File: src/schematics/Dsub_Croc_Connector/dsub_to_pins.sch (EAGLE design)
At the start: 39 parts

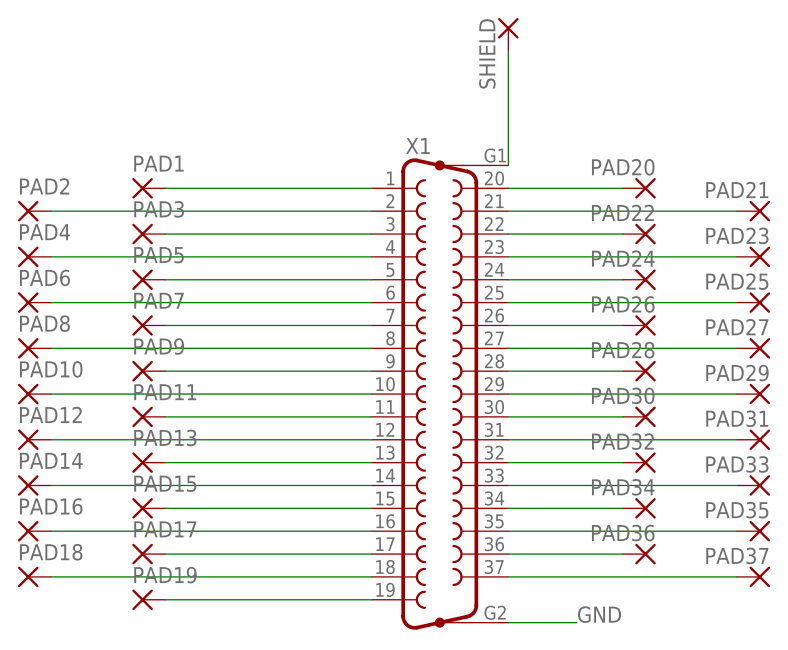
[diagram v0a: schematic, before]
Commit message: New Debug phantom, and new Dsub adaptors. With Gerbers sent to PCBWay
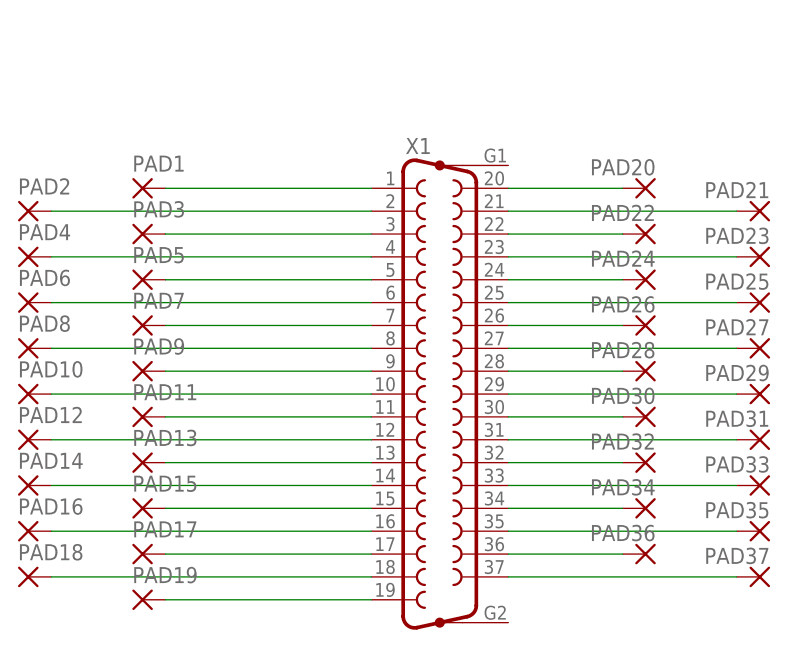
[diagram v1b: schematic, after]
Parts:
- removed SHIELD: WIREPAD3,81/1,3, wirepad:WIREPAD3,81/1,3
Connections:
- removed net GND: SHIELD.P, X1.G1, X1.G2
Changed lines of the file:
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@@
 <part name="PAD36" library="wirepad" deviceset="WIREPAD" device="3,81/1,3" value="WIREPAD3,81/1,3"/>
 <part name="PAD37" library="wirepad" deviceset="WIREPAD" device="3,81/1,3" value="WIREPAD3,81/1,3"/>
-<part name="SHIELD" library="wirepad" deviceset="WIREPAD" device="3,81/1,3" value="WIREPAD3,81/1,3"/>
 </parts>
 <sheets>
@@
 <attribute name="NAME" x="148.463" y="31.1658" size="1.778" layer="95" rot="R180"/>
 </instance>
-<instance part="SHIELD" gate="G$1" x="119.38" y="88.9" smashed="yes" rot="R270">
-<attribute name="NAME" x="116.1542" y="90.043" size="1.778" layer="95" rot="R270"/>
-</instance>
 </instances>
 <busses>
 </busses>
 <nets>
-<net name="GND" class="0">
-<segment>
-<pinref part="X1" gate="G$1" pin="G1"/>
-<pinref part="SHIELD" gate="G$1" pin="P"/>
-<wire x1="119.38" y1="73.66" x2="119.38" y2="86.36" width="0.1524" layer="91"/>
-</segment>
-<segment>
-<pinref part="X1" gate="G$1" pin="G2"/>
-<wire x1="119.38" y1="22.86" x2="127" y2="22.86" width="0.1524" layer="91"/>
-<label x="127" y="22.86" size="1.778" layer="95"/>
-</segment>
-</net>
 <net name="1" class="0">
 <segment>
